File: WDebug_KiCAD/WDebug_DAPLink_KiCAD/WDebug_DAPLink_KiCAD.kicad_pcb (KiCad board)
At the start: 2 copper layers, 55 x 34 mm, 36 parts, among them J1 Conn_01x04, J2 Conn_01x05, J3 Conn_01x05, J4 Conn_02x10_Odd_Even, P1 USB_C_Plug_USB2.0, U1 AZ1117-3.3, U2 STM32F103C8Tx, Y1 8MHz

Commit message: 修改电阻电容封装
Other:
- board text added: "20200101"
- board text added: "Chenweipeng"
- board text added: "WDebug_DAPLink_V1.0"
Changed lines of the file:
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@@
   (general
     (thickness 1.6)
-    (drawings 12)
+    (drawings 15)
     (tracks 453)
     (zones 0)
@@
     )
   )
+  (gr_text 20200101 (at 126.12878 94.68104) (layer B.SilkS)
+    (effects (font (size 1 1) (thickness 0.15)) (justify mirror))
+  )
+  (gr_text Chenweipeng (at 125.28042 92.37726) (layer B.SilkS)
+    (effects (font (size 1 1) (thickness 0.15)) (justify mirror))
+  )
+  (gr_text WDebug_DAPLink_V1.0 (at 118.08968 89.7001) (layer B.SilkS)
+    (effects (font (size 1.5 1.5) (thickness 0.15)) (justify mirror))
+  )
   (gr_line (start 93.974314 100.97008) (end 93.974314 110.00713) (layer Edge.Cuts) (width 0.05))

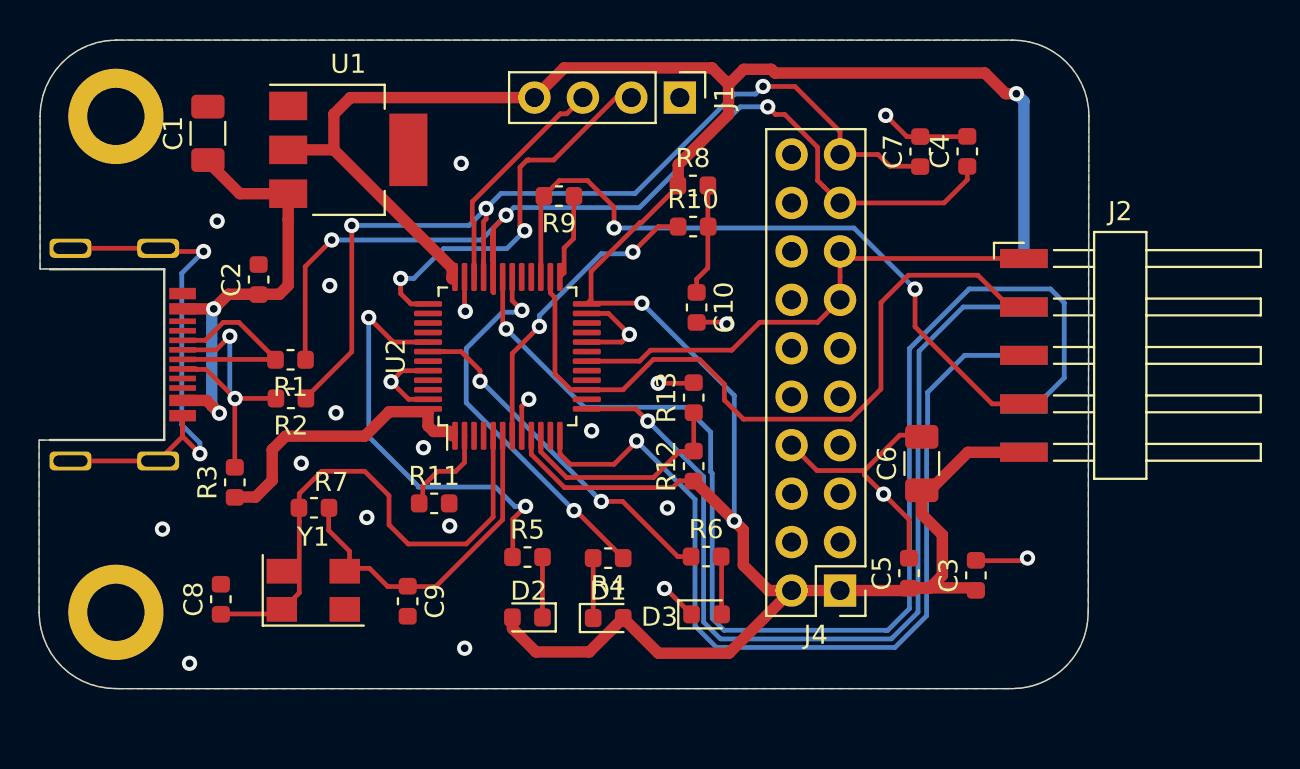
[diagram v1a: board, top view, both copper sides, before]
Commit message: 第二版可以正常烧写，有串口
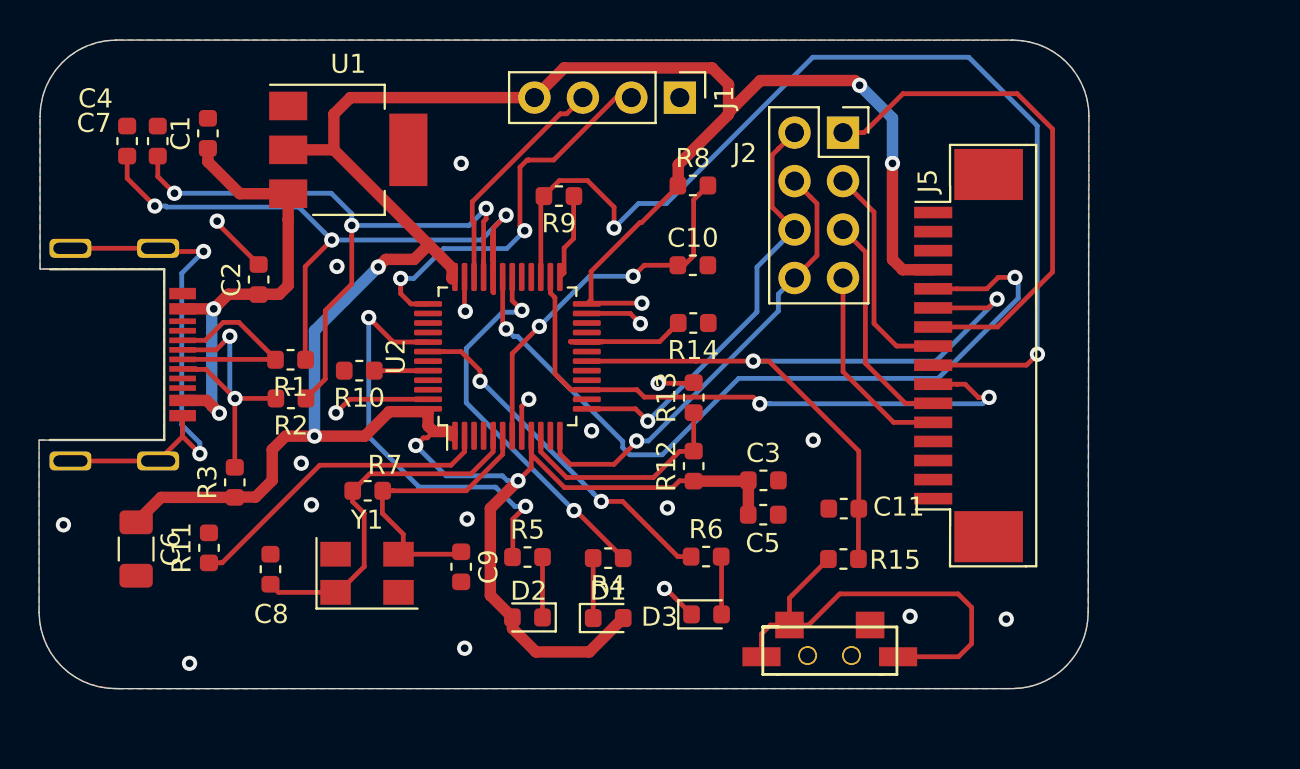
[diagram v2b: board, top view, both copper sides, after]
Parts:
- removed J3: Conn_01x05, Connector_Harwin:Harwin_M20-89005xx_1x05_P2.54mm_Horizontal
- removed J4: Conn_02x10_Odd_Even, Connector_PinHeader_2.54mm:PinHeader_2x10_P2.54mm_Vertical
- removed REF** (x2): hanpan, WDebug_KiCAD:hanpan
- added C11: 100nF, Capacitor_SMD:C_0603_1608Metric, F.Cu at (136.2, 104.6)
- added J5: Conn_01x18_Female, WDebug_KiCAD:1x16_P1.0mm, F.Cu at (143.5, 96.5)
- added R14: 10k, Resistor_SMD:R_0603_1608Metric, F.Cu at (128.3, 94.8)
- added R15: 100R, Resistor_SMD:R_0603_1608Metric, F.Cu at (136.1, 107.2)
- added SW1: SW_Rst, matrix_control_main:SWITCH_PUSH, F.Cu at (135.4, 111.5)
- C1: footprint Capacitor_SMD:C_1206_3216Metric -> Capacitor_SMD:C_0603_1608Metric
- J2: value Conn_01x05 -> Conn_02x04_UART_SW; footprint Connector_Harwin:Harwin_M20-89005xx_1x05_P2.54mm_Horizontal -> Connector_PinSocket_2.54mm:PinSocket_2x04_P2.54mm_Vertical
- R10, R8: value 100K -> 10K
- moved C4 44.0 mm to (98.6, 85.3)
- moved C6 41.4 mm to (99.1, 106.7), turned to 270 degrees
- moved C7 40.0 mm to (100.2, 85.3)
- moved R10 19.1 mm to (110.8, 97.3), turned to 180 degrees
- moved J2 19.0 mm to (136.1, 84.9)
- moved C3 12.2 mm to (131.9, 103.1), turned to 0 degrees
- moved R11 12.0 mm to (102.9, 106.6), turned to 90 degrees
- moved C5 8.23 mm to (131.9, 104.9), turned to 0 degrees
- moved C9 3.34 mm to (116.1, 107.6)
- moved C8 3.04 mm to (106.1, 107.7)
- moved R7 2.95 mm to (111.2, 103.6)
- moved Y1 2.95 mm to (111.2, 108.0)
- moved C10 2.22 mm to (128.2, 91.8), turned to 0 degrees
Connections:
- net /USB3+ renamed /USB_D+
- net /USB3- renamed /USB_D-
- C10 pad 1: Net-(C10-Pad1) -> /IF_RST
- J2 pad 1: /TG_RST -> /RX2
- J2 pad 2: /T_SWCLK -> /T_RX
- J2 pad 3: GND -> /TX2
- J2 pad 4: /T_SWDIO -> /T_TX
- J2 pad 5: +3V3 -> /RX1
- R10 pad 1: /IF_RST -> Net-(R10-Pad1)
- R10 pad 2: Net-(C10-Pad1) -> GND
- R8 pad 2: Net-(C10-Pad1) -> /IF_RST
- U2 pad 20: GND -> Net-(R14-Pad2)
- U2 pad 44: GND -> Net-(R10-Pad1)
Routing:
- net /RX2: track 0.00 -> 27.5 mm
- net /T_SWO: track 66.6 -> 41.7 mm, vias 1 -> 2
- net /T_RX: track 47.6 -> 22.7 mm
- net Net-(R15-Pad1): track 0.00 -> 23.7 mm
- net /T_TX: track 47.6 -> 24.1 mm
- net GND: track 40.2 -> 19.1 mm, vias 23 -> 20
- net /T_SWDIO: track 36.5 -> 55.3 mm
- net +3V3: track 167.0 -> 148.5 mm, vias 3 -> 7
- net /USB_D-: track 57.2 -> 39.6 mm
- net /USB_D+: track 49.0 -> 33.8 mm
- net /TG_RST: track 26.9 -> 39.6 mm, vias 0 -> 2
- net /RX1: track 0.00 -> 11.9 mm
- net /TX2: track 0.00 -> 11.7 mm
- net Net-(R11-Pad1): track 5.11 -> 16.7 mm
- net /TX1: track 0.00 -> 10.7 mm
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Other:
- board text added: "202003028"
- board text added: "WDebug_DAPLink_V1.1"
- board text removed: "20200101"
- board text removed: "Chenweipeng"
- board text removed: "WDebug_DAPLink_V1.0"

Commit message: WDebug——DAPLinkV1.2 调整中
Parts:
- removed R9: 100R, Resistor_SMD:R_0603_1608Metric
- added GND: hanpan, WDebug_KiCAD:hanpan, F.Cu at (98.8, 88.2)
- added J3: Conn_01x20_Female, WDebug_KiCAD:1x18_P1.0mm, F.Cu at (146.4, 97.1)
- added J4: Conn_01x05_Male, Connector_PinHeader_2.54mm:PinHeader_1x05_P2.54mm_Vertical, F.Cu at (133.6, 99.4)
- added REF**: hanpan, WDebug_KiCAD:hanpan, F.Cu at (100.7, 113.1)
- C6: footprint Capacitor_SMD:C_1206_3216Metric -> Capacitor_SMD:C_0603_1608Metric
- J2: footprint Connector_PinSocket_2.54mm:PinSocket_2x04_P2.54mm_Vertical -> Connector_PinHeader_2.54mm:PinHeader_2x04_P2.54mm_Vertical
- J5: moved to B.Cu
- Y1: footprint Crystal:Crystal_SMD_5032-4Pin_5.0x3.2mm -> Crystal:Crystal_SMD_3225-4Pin_3.2x2.5mm
- moved C3 33.1 mm to (102.0, 88.9)
- moved D3 22.7 mm to (106.3, 108.6)
- moved R6 22.6 mm to (106.3, 106.6)
- moved C6 19.5 mm to (102.0, 87.4), turned to 0 degrees
- moved C5 18.7 mm to (126.2, 87.0)
- moved C7 17.5 mm to (107.7, 101.2), turned to 270 degrees
- moved R5 16.8 mm to (103.2, 111.0), turned to 270 degrees
- moved R15 14.7 mm to (125.7, 96.8), turned to 180 degrees
- moved D1 14.0 mm to (109.9, 108.6)
- moved R4 13.8 mm to (110.0, 106.7)
- moved D2 13.5 mm to (106.2, 111.7), turned to 0 degrees
- moved R8 12.9 mm to (128.2, 100.5), turned to 180 degrees
- moved R10 12.7 mm to (100.8, 105.2)
- moved C4 11.7 mm to (107.7, 92.6)
- moved C10 10.8 mm to (128.2, 102.6)
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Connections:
- J5 pad 1: Net-(J5-Pad1) -> (no net)
- J5 pad 15: Net-(J5-Pad15) -> (no net)
- J5 pad 16: Net-(J5-Pad16) -> (no net)
- J5 pad 2: Net-(J5-Pad2) -> (no net)
- J5 pad 3: Net-(J5-Pad3) -> (no net)
- J5 pad 4: Net-(J5-Pad4) -> (no net)
- U1 pad 4: (no net) -> GND
- U2 pad 11: Net-(U2-Pad11) -> (no net)
- U2 pad 14: Net-(U2-Pad14) -> (no net)
- U2 pad 15: /T_SWCLK -> (no net)
- U2 pad 16: Net-(U2-Pad16) -> (no net)
- U2 pad 17: Net-(U2-Pad17) -> (no net)
- U2 pad 19: Net-(U2-Pad19) -> (no net)
- U2 pad 21: Net-(U2-Pad21) -> (no net)
- U2 pad 22: Net-(U2-Pad22) -> (no net)
- U2 pad 25: Net-(R9-Pad1) -> (no net)
- U2 pad 28: Net-(U2-Pad28) -> (no net)
- U2 pad 29: Net-(U2-Pad29) -> (no net)
- U2 pad 3: Net-(U2-Pad3) -> (no net)
- U2 pad 38: Net-(U2-Pad38) -> (no net)
- U2 pad 39: Net-(U2-Pad39) -> (no net)
- U2 pad 4: Net-(U2-Pad4) -> (no net)
- U2 pad 40: Net-(U2-Pad40) -> (no net)
- U2 pad 43: Net-(U2-Pad43) -> (no net)
- U2 pad 45: Net-(U2-Pad45) -> (no net)
- U2 pad 46: Net-(U2-Pad46) -> (no net)
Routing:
- net +3V3: track 148.5 -> 94.1 mm, vias 7 -> 5
- net /T_SWO: track 41.7 -> 0.00 mm, vias 2 -> 0
- net /T_SWDIO: track 55.3 -> 25.1 mm
- net /RX2: track 27.5 -> 0.01 mm
- net /USB_D-: track 39.6 -> 13.7 mm, vias 3 -> 0
- net /TG_RST: track 39.6 -> 21.4 mm, vias 2 -> 0
- net VBUS: track 24.3 -> 41.9 mm
- net /USB_D+: track 33.8 -> 17.1 mm, vias 3 -> 0
- net Net-(R11-Pad1): track 16.7 -> 4.67 mm
- net /RX1: track 11.9 -> 0.00 mm
- net /TX2: track 11.7 -> 0.00 mm
- net Net-(R10-Pad1): track 2.82 -> 14.5 mm, vias 0 -> 2
- net GND: track 19.1 -> 7.58 mm, vias 20 -> 3
- net /T_SWCLK: track 32.5 -> 21.7 mm
- net /TX1: track 10.7 -> 0.00 mm
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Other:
- board text added: "3V3"
- board text added: "CLK"
- board text added: "DIO"
- board text added: "GND"
- board text added: "RST"
- board text added: "RX1"
- board text added: "RX2"
- board text added: "TX1"
- board text added: "TX2"
- board text removed: "202003028"
- board text removed: "WDebug_DAPLink_V1.1"

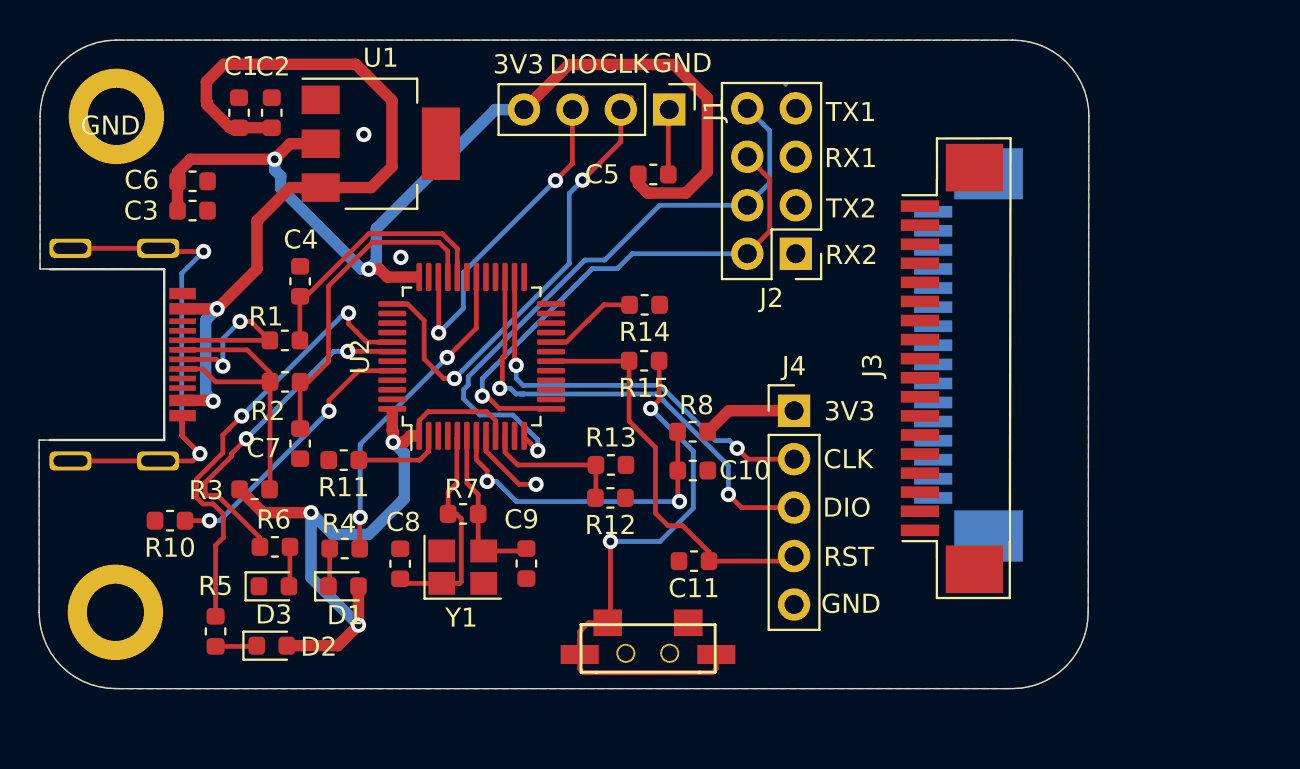
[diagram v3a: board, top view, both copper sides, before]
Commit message: 修改好DAPLinkV1.2版本
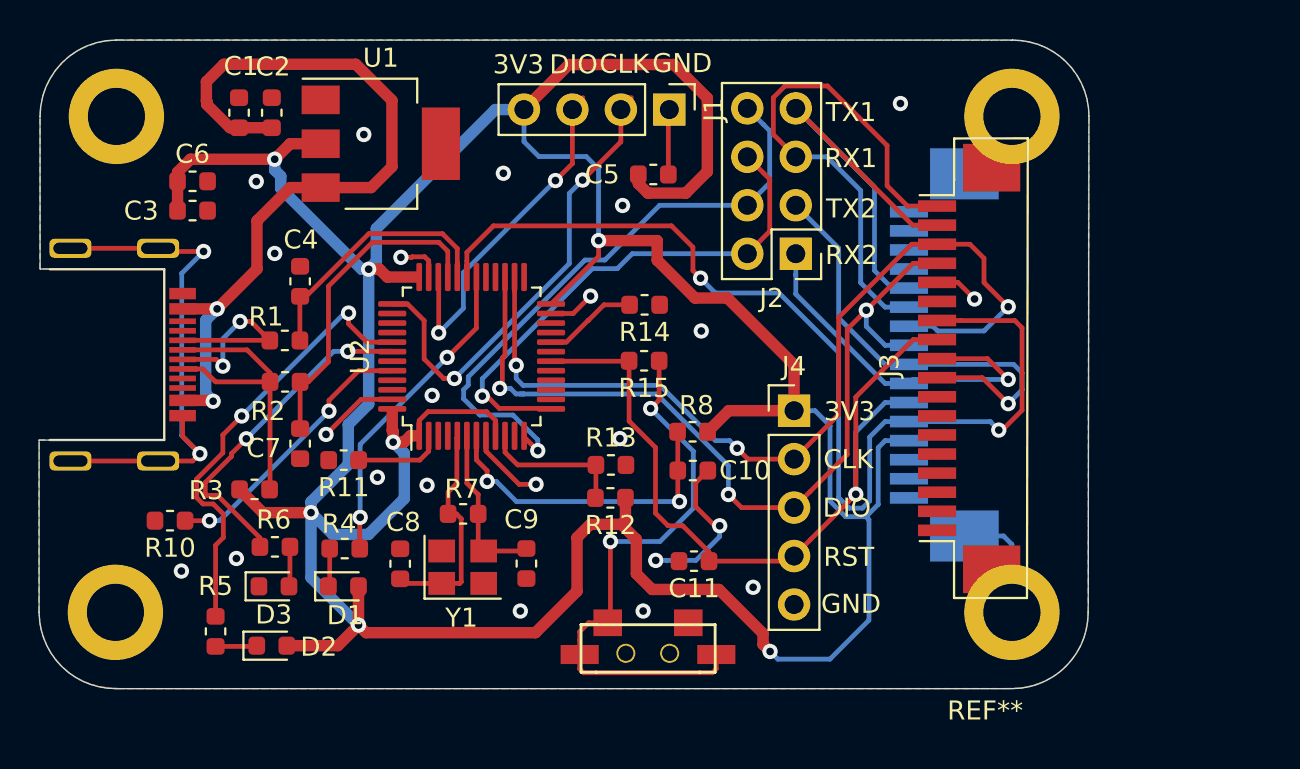
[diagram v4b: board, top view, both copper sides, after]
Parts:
- removed GND: hanpan, WDebug_KiCAD:hanpan
- removed the REF** at (100.7, 113.1)
- added REF**: hanpan, WDebug_DAPLink:hanpan, F.Cu at (143.6, 114.7)
- added REF**: hanpan, WDebug_DAPLink:hanpan, F.Cu at (143.0, 88.0)
- added REF**: hanpan, WDebug_DAPLink:hanpan, F.Cu at (98.1, 112.6)
- added REF**: hanpan, WDebug_DAPLink:hanpan, F.Cu at (98.1, 88.0)
- J5: value Conn_01x18_Female -> 01x18_Female_Fan
- moved J5 1.27 mm to (142.2, 96.5)
- moved J3 0.90 mm to (147.3, 97.1)
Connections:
- J3 pad 10: (no net) -> /RX2
- J3 pad 11: (no net) -> /TG_RST
- J3 pad 12: (no net) -> /T_SWO
- J3 pad 14: (no net) -> GND
- J3 pad 15: (no net) -> /T_SWDIO
- J3 pad 16: (no net) -> /T_SWCLK
- J3 pad 17: (no net) -> /TX1
- J3 pad 18: (no net) -> /RX1
- J3 pad 19: (no net) -> GND
- J3 pad 20: (no net) -> GND
- J3 pad 9: (no net) -> /TX2
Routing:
- net +3V3: track 94.1 -> 195.5 mm, vias 5 -> 7
- net /T_SWO: track 0.00 -> 55.7 mm, vias 0 -> 2
- net GND: track 7.58 -> 43.6 mm, vias 3 -> 23
- net /RX1: track 0.00 -> 28.3 mm
- net /T_SWCLK: track 21.7 -> 48.5 mm, vias 2 -> 3
- net /TX2: track 0.00 -> 23.9 mm, vias 0 -> 1
- net /TX1: track 0.00 -> 22.3 mm
- net /TG_RST: track 21.4 -> 43.2 mm, vias 0 -> 1
- net /T_SWDIO: track 25.1 -> 45.2 mm, vias 2 -> 3
- net /RX2: track 0.01 -> 19.5 mm, vias 0 -> 1
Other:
- board text added: "WDebug_DAPLink_V1.2 Chenweipeng 20200413"

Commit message: 提交修改USB type-C和按键 3D模型
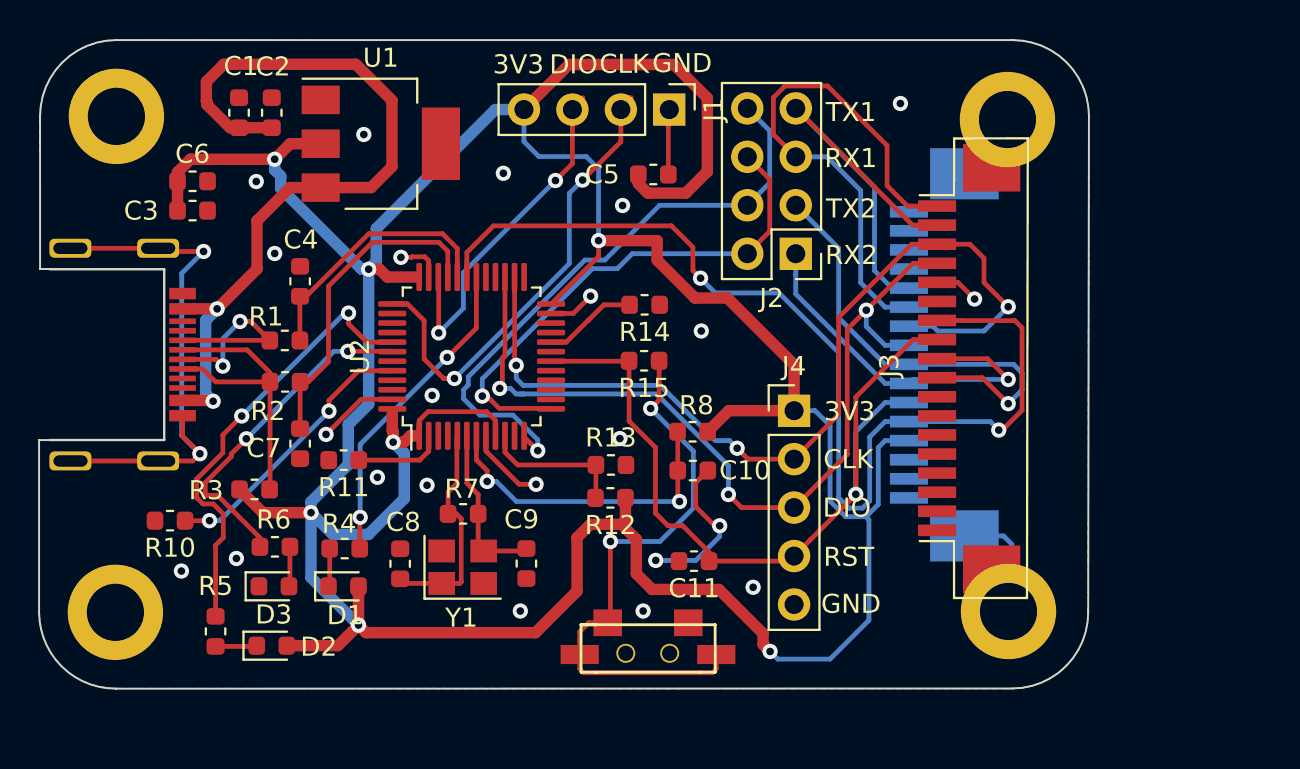
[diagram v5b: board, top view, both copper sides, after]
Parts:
- removed the REF** at (143.6, 114.7)
- removed the REF** at (143.0, 88.0)
- added REF**: hanpan, WDebug_DAPLink:hanpan, F.Cu at (144.8, 113.9)
- added REF**: hanpan, WDebug_DAPLink:hanpan, F.Cu at (144.8, 88.2)
- P1: footprint matrix_control_main:USB-Type-C -> WDebug_DAPLink:USB-Type-C
- SW1: footprint matrix_control_main:SWITCH_PUSH -> WDebug_DAPLink:SWITCH_PUSH
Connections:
- J3 pad 1: (no net) -> Net-(J3-Pad1)
- J3 pad 13: (no net) -> +3V3
- J3 pad 2: (no net) -> Net-(J3-Pad2)
- J3 pad 3: (no net) -> Net-(J3-Pad3)
- J3 pad 4: (no net) -> Net-(J3-Pad4)
- J3 pad 5: (no net) -> Net-(J3-Pad5)
- J3 pad 6: (no net) -> Net-(J3-Pad6)
- J3 pad 7: (no net) -> Net-(J3-Pad7)
- J3 pad 8: (no net) -> Net-(J3-Pad8)
- J5 pad 1: (no net) -> Net-(J5-Pad1)
- J5 pad 15: (no net) -> Net-(J5-Pad15)
- J5 pad 16: (no net) -> Net-(J5-Pad16)
- J5 pad 2: (no net) -> Net-(J5-Pad2)
- J5 pad 3: (no net) -> Net-(J5-Pad3)
- J5 pad 4: (no net) -> Net-(J5-Pad4)
- U1 pad 4: GND -> (no net)
- U2 pad 11: (no net) -> Net-(U2-Pad11)
- U2 pad 14: (no net) -> Net-(U2-Pad14)
- U2 pad 15: (no net) -> Net-(U2-Pad15)
- U2 pad 16: (no net) -> Net-(U2-Pad16)
- U2 pad 17: (no net) -> Net-(U2-Pad17)
- U2 pad 19: (no net) -> Net-(U2-Pad19)
- U2 pad 21: (no net) -> Net-(U2-Pad21)
- U2 pad 22: (no net) -> Net-(U2-Pad22)
- U2 pad 25: (no net) -> Net-(U2-Pad25)
- U2 pad 28: (no net) -> Net-(U2-Pad28)
- U2 pad 29: (no net) -> Net-(U2-Pad29)
- U2 pad 3: (no net) -> Net-(U2-Pad3)
- U2 pad 38: (no net) -> Net-(U2-Pad38)
- U2 pad 39: (no net) -> Net-(U2-Pad39)
- U2 pad 4: (no net) -> Net-(U2-Pad4)
- U2 pad 40: (no net) -> Net-(U2-Pad40)
- U2 pad 43: (no net) -> Net-(U2-Pad43)
- U2 pad 45: (no net) -> Net-(U2-Pad45)
- U2 pad 46: (no net) -> Net-(U2-Pad46)
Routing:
- net GND: track 43.6 -> 36.9 mm

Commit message: 解决框图生成模型问题
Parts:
- P1: footprint WDebug_DAPLink:USB-Type-C -> WDebug_KiCAD:USB-Type-C
- SW1: footprint WDebug_DAPLink:SWITCH_PUSH -> WDebug_KiCAD:SWITCH_PUSH
